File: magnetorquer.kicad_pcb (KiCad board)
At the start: 2 copper layers, 90.2 x 95.9 mm, 47 parts, among them J2 Conn_01x07_Female, SW1 SW_Push, U1 MSP430FR5994IPN, U2 LIS2DH12TR, U3 L3GD20HTR, U4 MP6515GF-Z, U5 MP6515GF-Z, U6 MP6515GF-Z, U7 DRV5055A4xLPGxQ1, U8 DRV5055A4xLPGxQ1, U9 DRV5055A4xLPGxQ1, Y1 Crystal, Y2 DNP

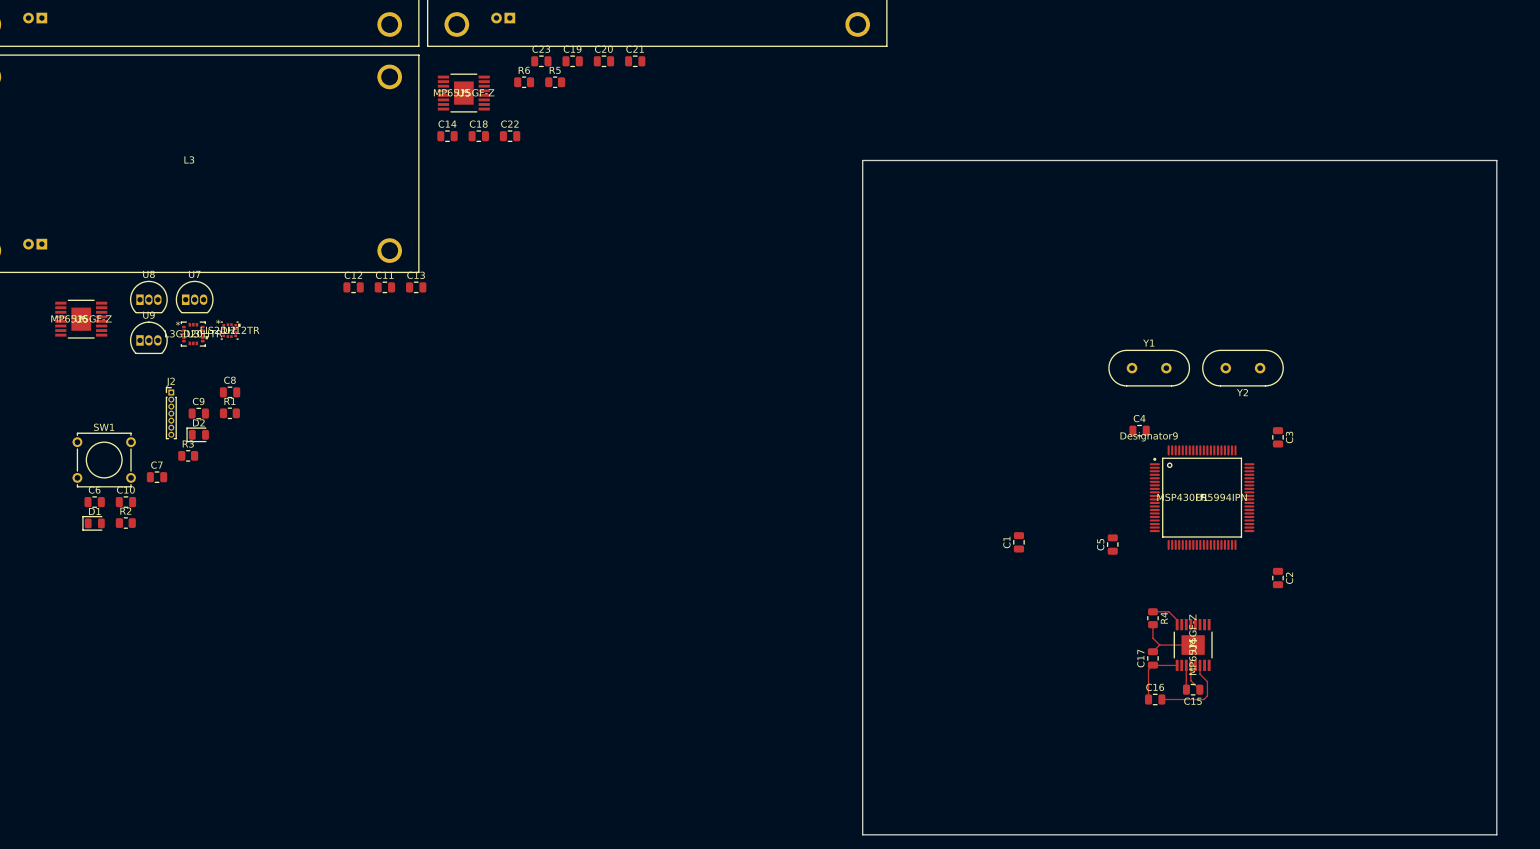
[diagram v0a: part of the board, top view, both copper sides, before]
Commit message: adicionado conector pc104
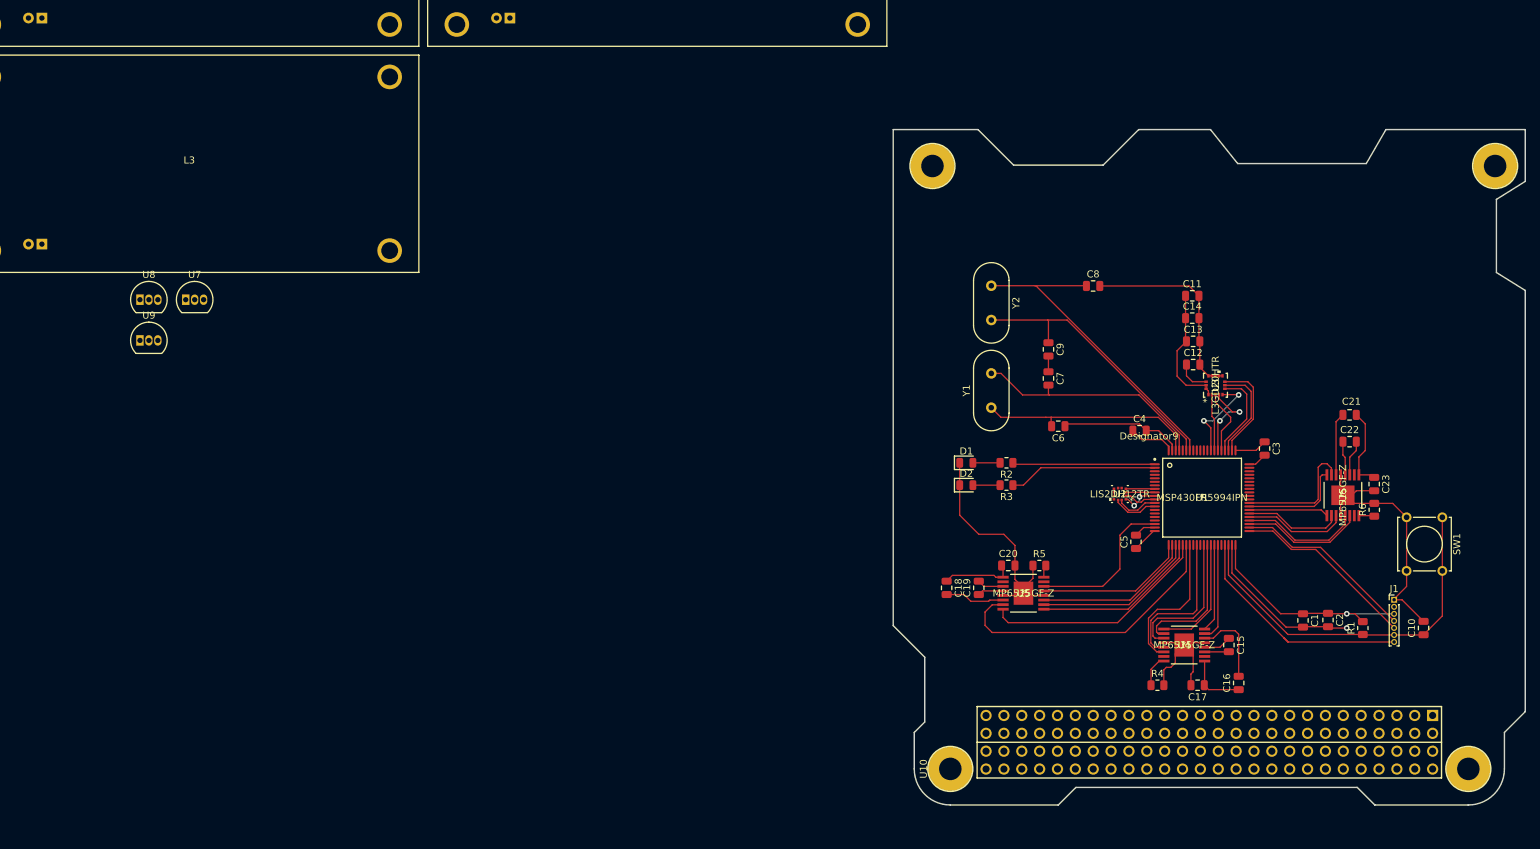
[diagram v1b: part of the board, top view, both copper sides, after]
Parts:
- removed J2: Conn_01x07_Female, Connector_PinHeader_1.00mm:PinHeader_1x07_P1.00mm_Vertical
- added J1: Conn_01x07_Female, Connector_PinHeader_1.00mm:PinHeader_1x07_P1.00mm_Vertical, F.Cu at (221.6, 127.6)
- added U10: Payload, magnetorque_lib:PC104-Standard, F.Cu at (232.2, 151.6)
- moved SW1 194.4 mm to (228.5, 115.8), turned to -90 degrees
- moved C10 185.4 mm to (225.8, 131.6), turned to 90 degrees
- moved U6 181.1 mm to (214.3, 112.7), turned to 90 degrees
- moved R1 164.0 mm to (217.2, 131.6), turned to 90 degrees
- moved U3 145.5 mm to (196.2, 97.0), turned to 90 degrees
- moved C6 137.4 mm to (173.9, 102.9), turned to 180 degrees
- moved R6 135.3 mm to (218.8, 114.8), turned to 90 degrees
- moved C23 132.8 mm to (218.8, 111.1), turned to -90 degrees
- moved U2 128.7 mm to (182.6, 112.5), turned to 180 degrees
- moved C7 127.5 mm to (172.5, 96.1), turned to -90 degrees
- moved C22 127.0 mm to (215.3, 105.1)
- moved R2 125.5 mm to (166.5, 108.1), turned to 180 degrees
- moved D1 124.2 mm to (160.8, 108.1)
- moved C8 123.7 mm to (178.8, 82.9)
- moved C9 121.2 mm to (172.5, 91.9), turned to -90 degrees
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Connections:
- U1 pad 12: H2_nFAULT -> ACCEL_INT1
- U1 pad 13: unconnected-(U1-Pad13) -> ACCEL_INT2
- U1 pad 15: H3_BREAK -> MAG_2
- U1 pad 18: unconnected-(U1-Pad18) -> H2_ENBL
- U1 pad 21: unconnected-(U1-Pad21) -> H2_nSLEEP
- U1 pad 22: unconnected-(U1-Pad22) -> H2_PHASE
- U1 pad 23: unconnected-(U1-Pad23) -> H2_BREAK
- U1 pad 24: unconnected-(U1-Pad24) -> H2_nFAULT
- U1 pad 25: unconnected-(U1-Pad25) -> H2_BMODE
- U1 pad 26: unconnected-(U1-Pad26) -> H2_VISEN
- U1 pad 27: H_nSLEEP -> H1_ENBL
- U1 pad 28: H1_VISEN -> unconnected-(U1-Pad28)
- U1 pad 29: H2_VISEN -> H1_nSLEEP
- U1 pad 30: H3_VISEN -> unconnected-(U1-Pad30)
- U1 pad 31: H1_BREAK -> H1_PHASE
- U1 pad 32: H1_PHASE -> H1_BREAK
- U1 pad 33: H1_BMODE -> H1_nFAULT
- U1 pad 34: H1_nFAULT -> H1_BMODE
- U1 pad 35: MAG_2 -> H1_VISEN
- U1 pad 4: ACCEL_INT1 -> unconnected-(U1-Pad4)
- U1 pad 43: unconnected-(U1-Pad43) -> H3_ENBL
- U1 pad 44: H3_PHASE -> H3_nSLEEP
- U1 pad 45: H3_BMODE -> H3_PHASE
- U1 pad 46: H3_nFAULT -> H3_BREAK
- U1 pad 47: GYRO_DEN -> H3_nFAULT
- U1 pad 48: H1_ENBL -> H3_BMODE
- U1 pad 49: H2_ENBL -> H3_VISEN
- U1 pad 5: ACCEL_INT2 -> unconnected-(U1-Pad5)
- U1 pad 50: H3_ENBL -> unconnected-(U1-Pad50)
- U1 pad 53: GYRO_MOSI -> unconnected-(U1-Pad53)
- U1 pad 54: GYRO_MISO -> unconnected-(U1-Pad54)
- U1 pad 55: GYRO_SCK -> unconnected-(U1-Pad55)
- U1 pad 56: GYRO_SCS -> unconnected-(U1-Pad56)
- U1 pad 57: H2_BREAK -> unconnected-(U1-Pad57)
- U1 pad 58: H2_PHASE -> unconnected-(U1-Pad58)
- U1 pad 59: H2_BMODE -> unconnected-(U1-Pad59)
- U1 pad 6: GYRO_INT1 -> MAG_1
- U1 pad 62: unconnected-(U1-Pad62) -> GYRO_DEN
- U1 pad 63: unconnected-(U1-Pad63) -> GYRO_INT2
- U1 pad 64: MAG_1 -> GYRO_INT1
- U1 pad 65: unconnected-(U1-Pad65) -> GYRO_MOSI
- U1 pad 66: unconnected-(U1-Pad66) -> GYRO_MISO
- U1 pad 67: unconnected-(U1-Pad67) -> GYRO_SCK
- U1 pad 68: unconnected-(U1-Pad68) -> GYRO_SCS
- U1 pad 7: GYRO_INT2 -> unconnected-(U1-Pad7)
- U4 pad 5: H_nSLEEP -> H1_nSLEEP
- U5 pad 5: H_nSLEEP -> H2_nSLEEP
- U6 pad 5: H_nSLEEP -> H3_nSLEEP
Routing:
- net GND: track 9.40 -> 171.7 mm, vias 0 -> 1
- net +3V3: track 8.61 -> 94.9 mm, vias 0 -> 1
- net SBWTDIO: track 0.00 -> 53.4 mm
- net Net-(C8-Pad1): track 0.00 -> 46.2 mm
- net H2_VISEN: track 0.00 -> 41.3 mm
- net Net-(C9-Pad1): track 0.00 -> 39.6 mm
- net Net-(C7-Pad2): track 0.00 -> 34.0 mm
- net SBWTCK: track 0.00 -> 33.4 mm
- net H2_BMODE: track 0.00 -> 32.7 mm
- net Net-(C6-Pad2): track 0.00 -> 31.3 mm
- net BCLUART_TXD: track 0.00 -> 26.6 mm
- net BCLUART_RXD: track 0.00 -> 26.1 mm
- net H2_nFAULT: track 0.00 -> 24.1 mm
- net H2_BREAK: track 0.00 -> 23.4 mm
- net H2_PHASE: track 0.00 -> 22.6 mm
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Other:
- board size 90.2 x 95.9 mm -> 89.9 x 96 mm

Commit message: last commit
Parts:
- added REF**: bobinas, magnetorque_lib:bobinas, F.Cu at (166.2, 144.0)
- moved U7 289.0 mm to (325.0, -3.21)
- moved U8 113.6 mm to (152.6, 54.2)
- moved L1 93.0 mm to (93.4, 123.4)
- moved L3 91.2 mm to (140.3, 80.4), turned to 90 degrees
- moved L2 88.6 mm to (95.6, 109.5), turned to 90 degrees
- moved U2 81.5 mm to (101.7, 102.7)
- moved C21 80.8 mm to (136.9, 81.8)
- moved C22 80.8 mm to (136.9, 85.6)
- moved C23 80.8 mm to (140.4, 91.6)
- moved R6 80.8 mm to (140.4, 95.3)
- moved U6 80.8 mm to (136.0, 93.2)
- moved C10 76.3 mm to (150.2, 121.9)
- moved C2 76.3 mm to (136.6, 120.7)
- moved J1 76.3 mm to (146.0, 117.8)
- moved SW1 76.3 mm to (152.8, 106.1)
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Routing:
- net H1_OUT2: track 0.00 -> 31.4 mm, vias 0 -> 1
- net H3_OUT1: track 0.00 -> 25.1 mm
- net H1_OUT1: track 0.00 -> 22.2 mm
- net H2_OUT2: track 0.00 -> 20.5 mm, vias 0 -> 1
- net H3_OUT2: track 0.00 -> 16.3 mm, vias 0 -> 1
- net H2_OUT1: track 0.00 -> 7.57 mm
- net ACCEL_INT2: track 6.48 -> 12.6 mm
- net ACCEL_INT1: track 5.97 -> 11.9 mm
- net ACCEL_SCK: track 5.36 -> 10.9 mm
- net ACCEL_MISO: track 4.11 -> 9.63 mm
- net ACCEL_MOSI: track 4.11 -> 9.62 mm
- net ACCEL_SCS: track 4.64 -> 10.1 mm
- net GND: track 171.7 -> 167.9 mm
- net H3_VISEN: track 17.9 -> 21.2 mm
- net H3_BMODE: track 14.8 -> 18.0 mm
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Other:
- outline, holes or cut-outs redrawn
